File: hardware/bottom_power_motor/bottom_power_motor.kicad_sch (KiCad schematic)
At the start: 102 parts, among them J1 Power/Motor 6p, J2 J_STK_A, J3 J_STK_B, Q1 P-FET 40V 30A, U1 L78L12, U2 TPS54360, U2_CB 100n, U2_CO 47u, U2_CZ 3n3, U2_D 60V 3A, U2_L 10u, U2_RC 10k, U2_RH 53k6, U2_RL 10k2, U2_RT_R 100k, U3 TLV62569, U4 TPS54360, U4_CB 100n, U4_CO 22u, U4_CZ 3n3, U4_D 60V 3A, U4_L 33u, U4_RC 10k, U4_RH 68k1, U4_RL 10k0, U4_RT_R 100k

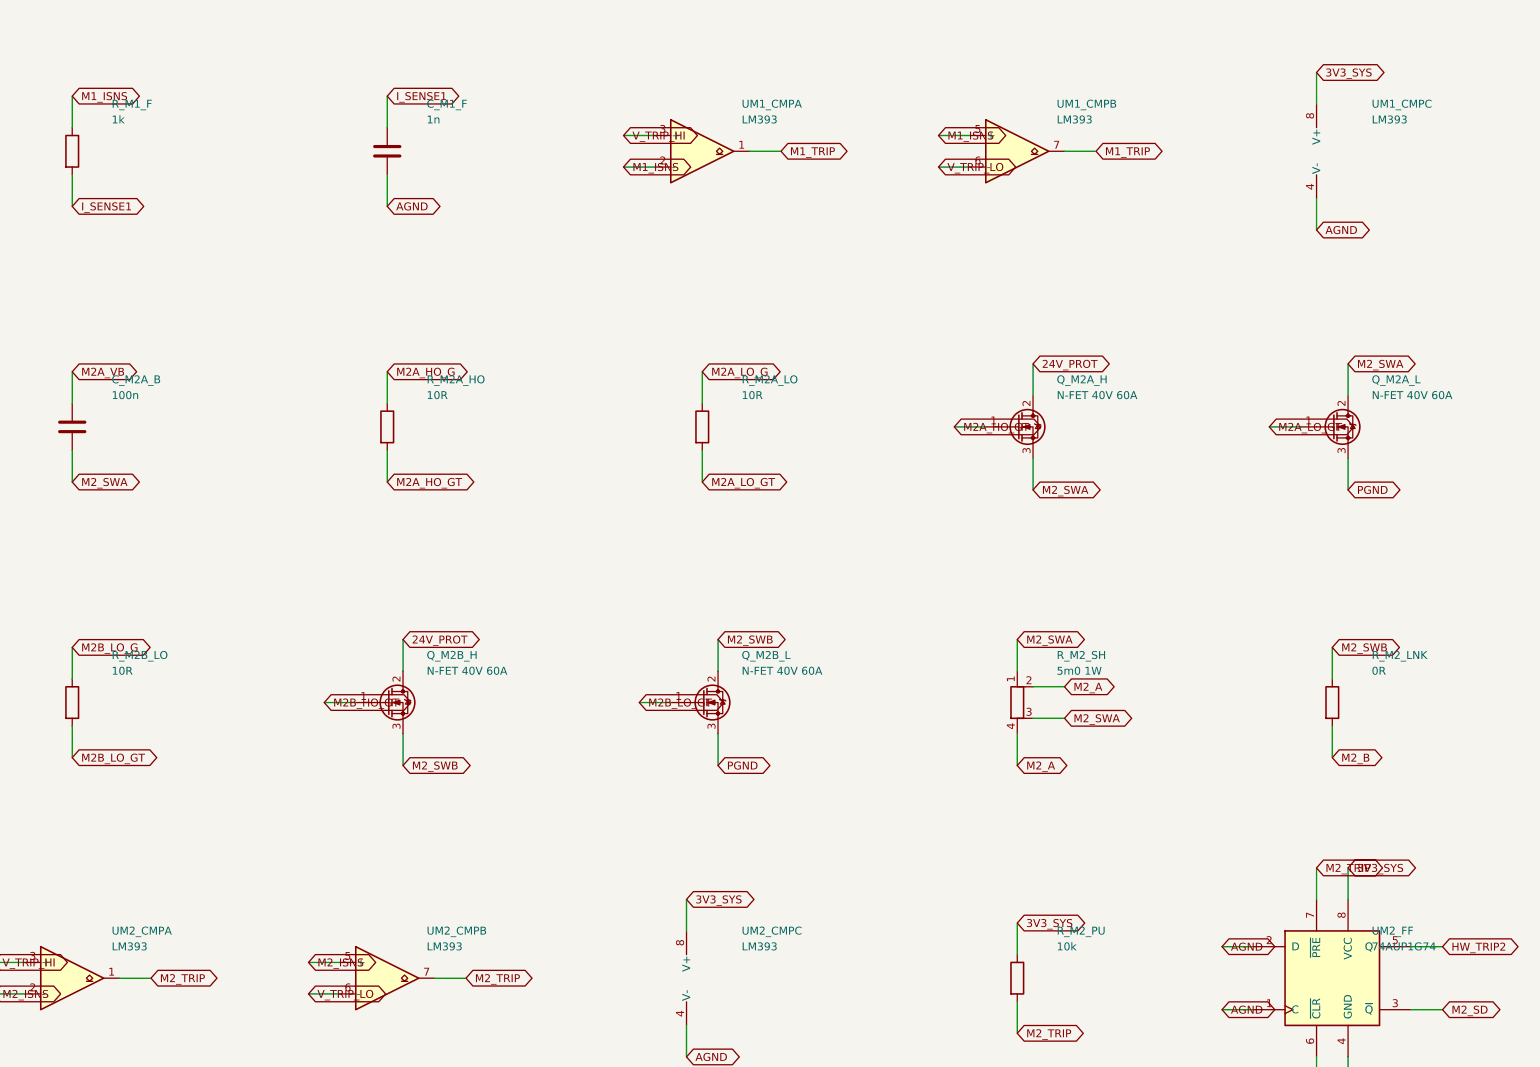
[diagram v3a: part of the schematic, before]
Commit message: TLV3702 statt LM393; Auslegung auf den kleinsten gemessenen Wert (14 Ohm)
ZWEI SACHEN IN EINEM COMMIT, weil beide aus derselben Messreihe kommen.

1) M6 vollstaendig: 16,5 / 20 / 14 Ohm. Die Streuung ist der erwartete
   Buersteneffekt - je nach Laeuferstellung liegen unterschiedlich viele
   Lamellen im Strompfad. Fuer die Auslegung zaehlt das Minimum, und das sind
   jetzt 14 Ohm statt der 15,0 Ohm aus M3. Damit steigt der Blockierstrom von
   1,6 auf 1,7 A, der Summenpfad von 3,9 auf 4,1 A und die Maximalaufnahme je
   Motor von 38 auf 41 W.

   Kein Bauteil aendert sich: Ausgelegt war ohnehin auf 2 A, der Trip liegt bei
   4,4 A (Faktor 2,6), die Sicherung bei 6,3 A. Die Zahlen sind nur ueberall
   konsistent nachgezogen.

   Damit ist der Blockierstrom dreifach unabhaengig bestaetigt - 2 V, 24 V
   blockiert, Multimeter - und der Faktor-2-Irrtum ausgeschlossen.

2) Punkt 57 geloest, und zwar OHNE die geroutete Platine anzufassen.

   Der Weg ueber 5V_SYS, den der Nutzer zunaechst gewaehlt hatte, scheiterte an
   der Geometrie: Das Netz liegt komplett auf der linken Boardhaelfte, die
   Komparatoren rechts - 27,3 bzw. 36,0 mm entfernt, zwei lange Bahnen ueber
   985 vorhandene Segmente. 12V_GATE waere mit 3-7 mm nah, ist aber die
   lauteste Schiene der Platine, und der Komparator hat keinen eigenen
   Abblockkondensator.

   Gewaehlt: TLV3702. Rail-to-Rail-Eingang, Open-Drain, SOIC-8 im
   Standard-Pinout eines dualen Komparators. Gleicher Footprint, gleiche Netze,
   keine Leiterbahn angefasst, DRC unveraendert (228 Meldungen, alle
   Bestueckungsdruck; 61 offene Verbindungen wie zuvor). Er bleibt an 3,3 V und
   damit auf derselben Schiene wie die INA240-Referenz, was die ratiometrische
   Kopplung der Trip-Schwelle erhaelt. Mit rund 5 us ist er langsamer als der
   LM393 - hier ein Vorteil, weil der Komparator das ungefilterte Sense-Signal
   sieht und an einem Latch haengt (Punkt 59).

   ACHTUNG fuer die Bestellung: KiCad 10 bringt kein TLV-Symbol mit, im
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
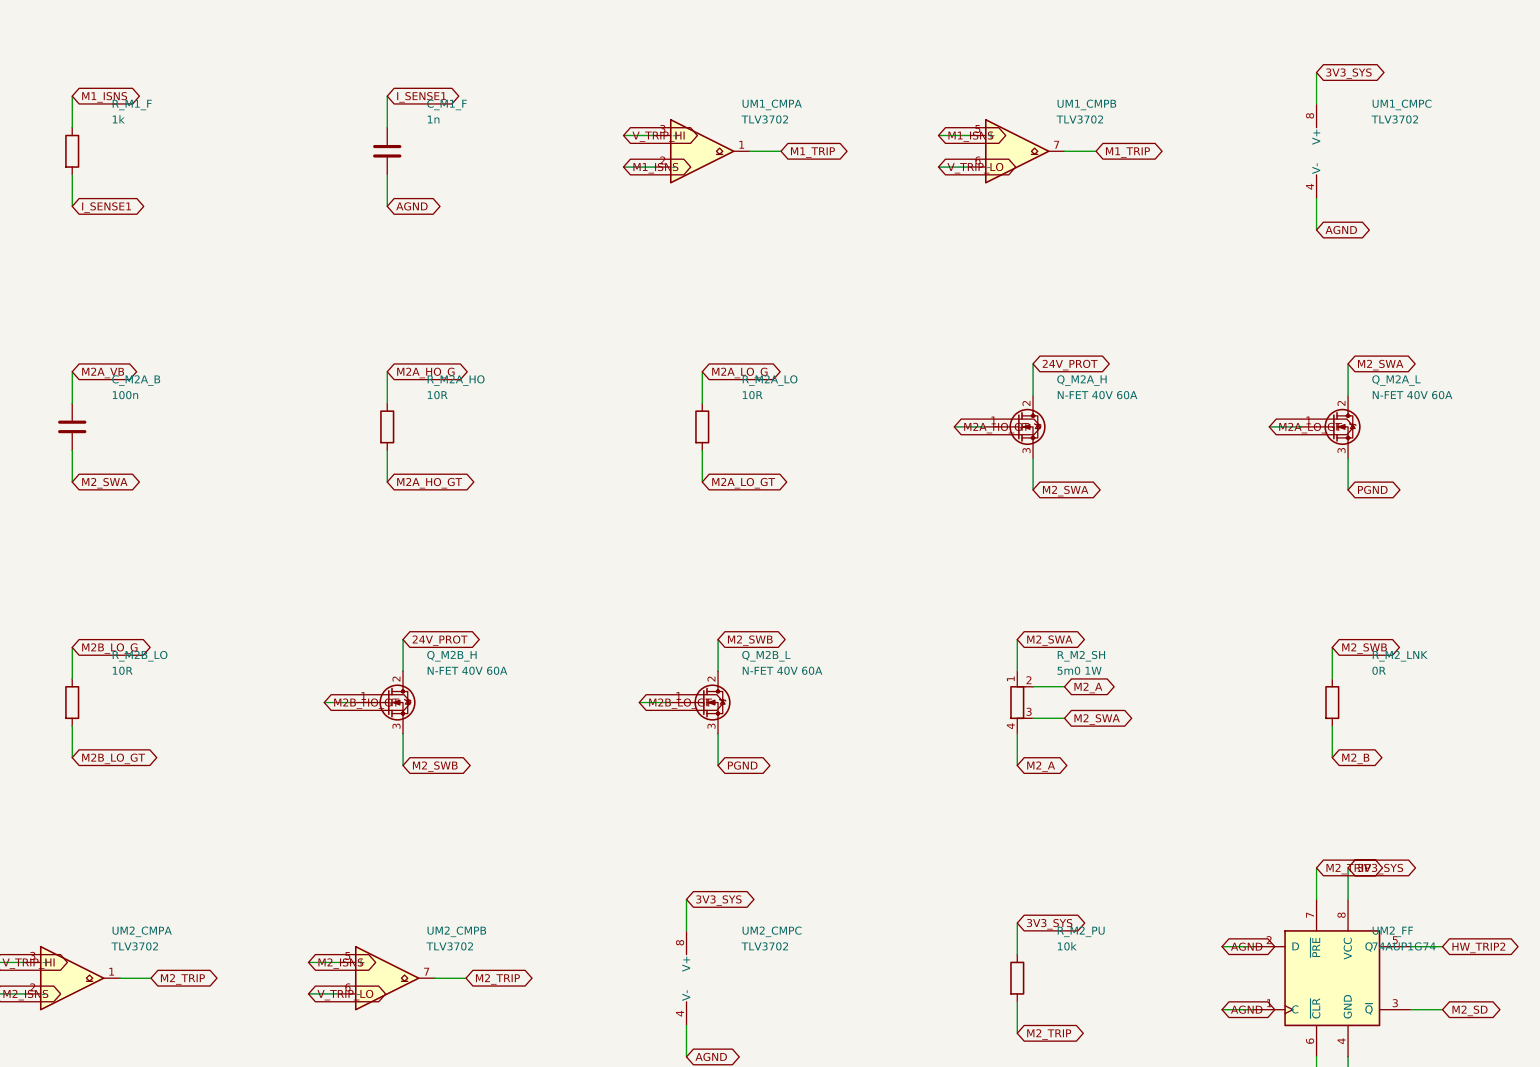
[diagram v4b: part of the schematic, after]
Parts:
- UM1_CMP, UM2_CMP: value LM393 -> TLV3702; MPN (none) -> Rail-to-Rail-Eingang + Open-Drain PFLICHT - kein LM393
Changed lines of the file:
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@@
     (property "Reference" "UM1_CMP" (at 234.9500 328.9300 0)
       (effects (font (size 1.27 1.27)) (justify left)))
-    (property "Value" "LM393" (at 234.9500 331.4700 0)
+    (property "Value" "TLV3702" (at 234.9500 331.4700 0)
       (effects (font (size 1.27 1.27)) (justify left)))
     (property "Footprint" "Package_SO:SOIC-8_3.9x4.9mm_P1.27mm" (at 228.6000 336.5500 0)
       (effects (font (size 1.27 1.27)) hide))
+    (property "MPN" "Rail-to-Rail-Eingang + Open-Drain PFLICHT - kein LM393" (at 228.6000 339.0900 0)
+      (effects (font (size 1.27 1.27)) hide))
     (pin "1")
     (pin "2")
@@
     (property "Reference" "UM1_CMP" (at 285.7500 328.9300 0)
       (effects (font (size 1.27 1.27)) (justify left)))
-    (property "Value" "LM393" (at 285.7500 331.4700 0)
+    (property "Value" "TLV3702" (at 285.7500 331.4700 0)
       (effects (font (size 1.27 1.27)) (justify left)))
     (property "Footprint" "Package_SO:SOIC-8_3.9x4.9mm_P1.27mm" (at 279.4000 336.5500 0)
       (effects (font (size 1.27 1.27)) hide))
+    (property "MPN" "Rail-to-Rail-Eingang + Open-Drain PFLICHT - kein LM393" (at 279.4000 339.0900 0)
+      (effects (font (size 1.27 1.27)) hide))
     (pin "5")
     (pin "6")
@@
     (property "Reference" "UM1_CMP" (at 336.5500 328.9300 0)
       (effects (font (size 1.27 1.27)) (justify left)))
-    (property "Value" "LM393" (at 336.5500 331.4700 0)
+    (property "Value" "TLV3702" (at 336.5500 331.4700 0)
       (effects (font (size 1.27 1.27)) (justify left)))
     (property "Footprint" "Package_SO:SOIC-8_3.9x4.9mm_P1.27mm" (at 330.2000 336.5500 0)
       (effects (font (size 1.27 1.27)) hide))
+    (property "MPN" "Rail-to-Rail-Eingang + Open-Drain PFLICHT - kein LM393" (at 330.2000 339.0900 0)
+      (effects (font (size 1.27 1.27)) hide))
     (pin "4")
     (pin "8")
@@
     (property "Reference" "UM2_CMP" (at 133.3500 462.2800 0)
       (effects (font (size 1.27 1.27)) (justify left)))
-    (property "Value" "LM393" (at 133.3500 464.8200 0)
+    (property "Value" "TLV3702" (at 133.3500 464.8200 0)
       (effects (font (size 1.27 1.27)) (justify left)))
     (property "Footprint" "Package_SO:SOIC-8_3.9x4.9mm_P1.27mm" (at 127.0000 469.9000 0)
       (effects (font (size 1.27 1.27)) hide))
+    (property "MPN" "Rail-to-Rail-Eingang + Open-Drain PFLICHT - kein LM393" (at 127.0000 472.4400 0)
+      (effects (font (size 1.27 1.27)) hide))
     (pin "1")
     (pin "2")
@@
     (property "Reference" "UM2_CMP" (at 184.1500 462.2800 0)
       (effects (font (size 1.27 1.27)) (justify left)))
-    (property "Value" "LM393" (at 184.1500 464.8200 0)
+    (property "Value" "TLV3702" (at 184.1500 464.8200 0)
       (effects (font (size 1.27 1.27)) (justify left)))
     (property "Footprint" "Package_SO:SOIC-8_3.9x4.9mm_P1.27mm" (at 177.8000 469.9000 0)
       (effects (font (size 1.27 1.27)) hide))
+    (property "MPN" "Rail-to-Rail-Eingang + Open-Drain PFLICHT - kein LM393" (at 177.8000 472.4400 0)
+      (effects (font (size 1.27 1.27)) hide))
     (pin "5")
     (pin "6")
@@
     (property "Reference" "UM2_CMP" (at 234.9500 462.2800 0)
       (effects (font (size 1.27 1.27)) (justify left)))
-    (property "Value" "LM393" (at 234.9500 464.8200 0)
+    (property "Value" "TLV3702" (at 234.9500 464.8200 0)
       (effects (font (size 1.27 1.27)) (justify left)))
     (property "Footprint" "Package_SO:SOIC-8_3.9x4.9mm_P1.27mm" (at 228.6000 469.9000 0)
       (effects (font (size 1.27 1.27)) hide))
-    (pin "4")
+    (property "MPN" "Rail-to-Rail-Eingang + Open-Drain PFLICHT - kein LM393" (at 228.6000 472.4400 0)
+      (effects (font (size 1.27 1.27)) hide))
+    (pin "4")

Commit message: Eigenes TLV3702-Symbol statt fremder lib_id
Der Schaltplan trug bisher Comparator:LM393 als lib_id und TLV3702 als Wert -
technisch folgenlos, weil die Pinbelegung identisch ist, aber eine Falle fuer
den naechsten Leser: Wer die lib_id liest, bestellt einen LM393, dessen
Gleichtaktbereich bei 3,3 V eben nicht reicht.

Jetzt liegt ein richtig benanntes Symbol in hardware/lib/SwitchStack.kicad_sym,
erzeugt aus dem geometrisch identischen LM393-Symbol - die Pinbelegung ist
damit nachweislich das Standard-Pinout eines dualen Komparators:

  1 = OUT_A   2 = IN_A-   3 = IN_A+   4 = V-
  5 = IN_B+   6 = IN_B-   7 = OUT_B   8 = V+

Beschreibung, Datenblattlink und Suchbegriffe zeigen auf den TLV3702, der
Footprintfilter auf SOIC-8. Im Symbolkommentar steht, warum es das Symbol
ueberhaupt gibt und dass der Open-Drain-Ausgang Pflicht ist.

Geprueft: gen_bottom_sch.py laeuft, Netzlistenvergleich BESTANDEN.

Co-Authored-By: Claude Opus 5 (1M context) <noreply@anthropic.com>
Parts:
- UM1_CMP, UM2_CMP: symbol Comparator:LM393 -> SwitchStack:TLV3702
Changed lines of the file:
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@@
       (reference "C_M1_F") (unit 1))))
   )
-  (symbol (lib_id "Comparator:LM393") (at 228.6000 336.5500 0) (unit 1)
+  (symbol (lib_id "SwitchStack:TLV3702") (at 228.6000 336.5500 0) (unit 1)
     (in_bom yes) (on_board yes) (dnp no)
     (property "Reference" "UM1_CMP" (at 234.9500 328.9300 0)
@@
       (reference "UM1_CMP") (unit 1))))
   )
-  (symbol (lib_id "Comparator:LM393") (at 279.4000 336.5500 0) (unit 2)
+  (symbol (lib_id "SwitchStack:TLV3702") (at 279.4000 336.5500 0) (unit 2)
     (in_bom yes) (on_board yes) (dnp no)
     (property "Reference" "UM1_CMP" (at 285.7500 328.9300 0)
@@
       (reference "UM1_CMP") (unit 2))))
   )
-  (symbol (lib_id "Comparator:LM393") (at 330.2000 336.5500 0) (unit 3)
+  (symbol (lib_id "SwitchStack:TLV3702") (at 330.2000 336.5500 0) (unit 3)
     (in_bom yes) (on_board yes) (dnp no)
     (property "Reference" "UM1_CMP" (at 336.5500 328.9300 0)
@@
       (reference "C_M2_F") (unit 1))))
   )
-  (symbol (lib_id "Comparator:LM393") (at 127.0000 469.9000 0) (unit 1)
+  (symbol (lib_id "SwitchStack:TLV3702") (at 127.0000 469.9000 0) (unit 1)
     (in_bom yes) (on_board yes) (dnp no)
     (property "Reference" "UM2_CMP" (at 133.3500 462.2800 0)
@@
       (reference "UM2_CMP") (unit 1))))
   )
-  (symbol (lib_id "Comparator:LM393") (at 177.8000 469.9000 0) (unit 2)
+  (symbol (lib_id "SwitchStack:TLV3702") (at 177.8000 469.9000 0) (unit 2)
     (in_bom yes) (on_board yes) (dnp no)
     (property "Reference" "UM2_CMP" (at 184.1500 462.2800 0)
@@
       (reference "UM2_CMP") (unit 2))))
   )
-  (symbol (lib_id "Comparator:LM393") (at 228.6000 469.9000 0) (unit 3)
+  (symbol (lib_id "SwitchStack:TLV3702") (at 228.6000 469.9000 0) (unit 3)
     (in_bom yes) (on_board yes) (dnp no)
     (property "Reference" "UM2_CMP" (at 234.9500 462.2800 0)

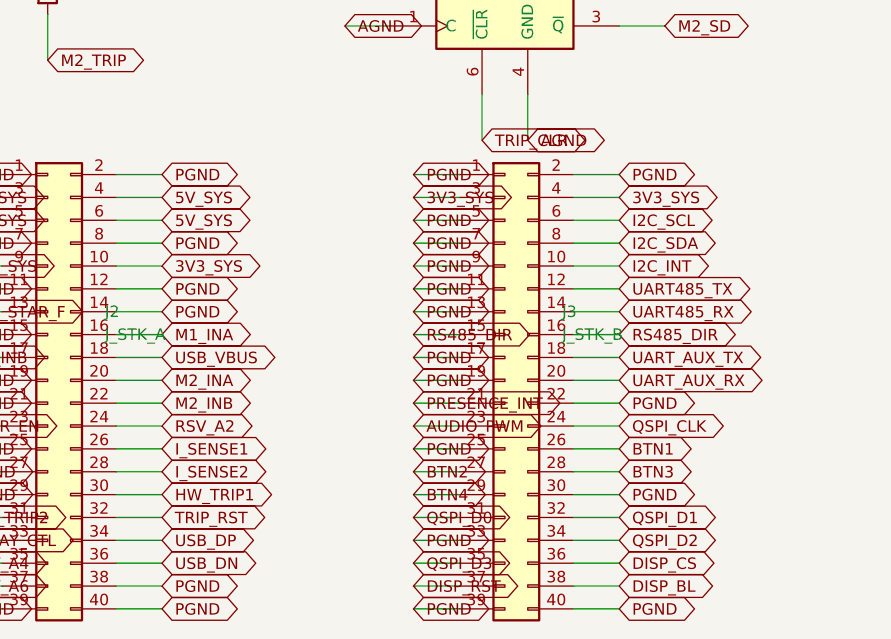
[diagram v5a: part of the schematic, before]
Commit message: Stack-Pinout v0.5: Tasten und I2C auf die Aussenreihe, Tasten auf beide Verbinder
Zwei Autorouter (1.9.0 und 2.3.0) und zwei Lagenzahlen hatten auf Top exakt
dieselben elf offenen Netze hinterlassen. Das ist kein Werkzeugproblem,
sondern die Pinbelegung.

BTN1..BTN4 lagen auf B26..B29 - vier benachbarten Kontakten der INNENreihe
des RECHTEN Verbinders. Ihre Taster sitzen aber in allen vier Ecken des
Top-Boards, zwei davon links. Zwei Bahnen mussten quer ueber ein Board mit
80 Steckkontakten im 1,27-mm-Raster, und alle vier zuerst aus der Innenreihe
heraus. I2C_SCL/SDA lagen ebenfalls innen.

Neu liegt jedes Tastennetz auf der AUSSENreihe des Verbinders, der seiner
Ecke am naechsten ist - von dort geht es direkt nach aussen und am Boardrand
entlang zum Taster:

  BTN1  B26 -> B1    aussen, y = -14,06   SW1 (+18 / -20)
  BTN2  B27 -> A2    aussen, y = -14,06   SW2 (-18 / -20)
  BTN3  B28 -> A40   aussen, y = +10,07   SW3 (-18 / +20)
  BTN4  B29 -> B39   aussen, y = +10,07   SW4 (+18 / +20)

  I2C_SCL  B6 -> B5  aussen
  I2C_SDA  B8 -> B7  aussen

Beide I2C-Teilnehmer auf Top - SHT4x und ToF - sitzen an der oberen Kante,
also dort, wo die neuen Pins liegen.

Die freigewordenen Kontakte B6, B8, B26..B29 werden PGND. Vier PGND-Pins sind
weggefallen (A2, A40, B1, B39); ueber beide Verbinder bleiben 25.

Alle drei Schaltplaene und Layouts neu erzeugt, Netzlistenvergleich bestanden,
keine Platzierungsfehler. Das Routing folgt.

Co-Authored-By: Claude Opus 5 (1M context) <noreply@anthropic.com>
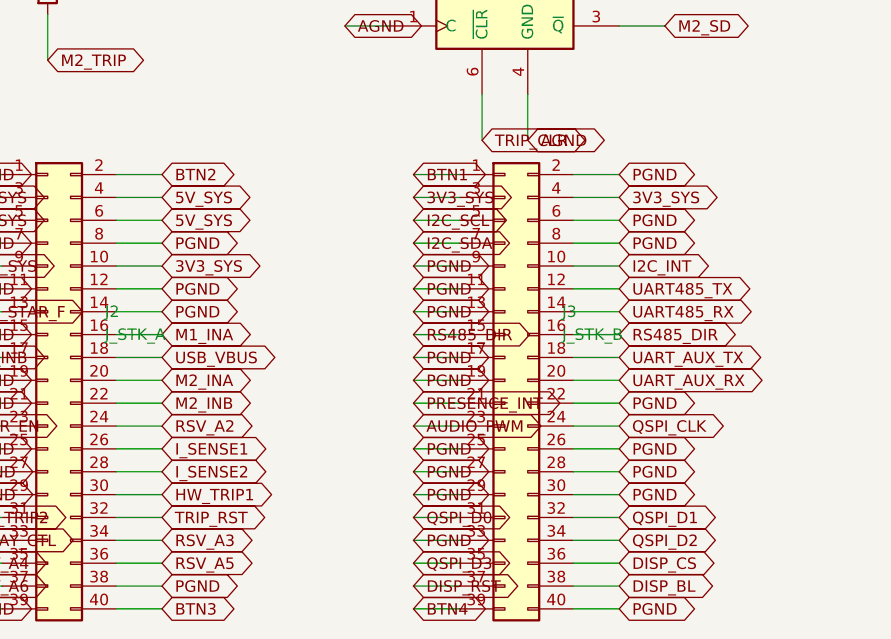
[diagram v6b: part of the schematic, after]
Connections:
- net BTN1: now also J3.1 (Pin_1); no longer J3.26 (Pin_26)
- net BTN2: now also J2.2 (Pin_2); no longer J3.27 (Pin_27)
- net BTN3: now also J2.40 (Pin_40); no longer J3.28 (Pin_28)
- net BTN4: now also J3.39 (Pin_39); no longer J3.29 (Pin_29)
- net I2C_SCL: now also J3.5 (Pin_5); no longer J3.6 (Pin_6)
- net I2C_SDA: now also J3.7 (Pin_7); no longer J3.8 (Pin_8)
- net PGND: now also J3.26 (Pin_26), J3.27 (Pin_27), J3.28 (Pin_28), J3.29 (Pin_29), J3.6 (Pin_6), J3.8 (Pin_8); no longer J2.2 (Pin_2), J2.40 (Pin_40), J3.1 (Pin_1), J3.39 (Pin_39), J3.5 (Pin_5), J3.7 (Pin_7)
- net USB_DN renamed RSV_A5
- net USB_DP renamed RSV_A3
